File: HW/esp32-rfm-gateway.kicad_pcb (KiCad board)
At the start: 2 copper layers, 99 x 93.5 mm, 97 parts, among them J1 ph_1x2, J10 CS_1, J11 CS_1, J12 CS_1, J13 CS_1, J14 CS_1, J2 ph_1x2, J20 220V~, J21 ph_1x2, J22 s14500, J23 s18650, J24 ph_1x3, J25 ph_1x2, J3 ph_1x3, J30 AntSMA, J4 ph_1x4, J40 ph_1x2, J5 ph_1x4, J6 ph_1x3, J7 ph_1x4, J8 ph_1x4, Q20 IRLML2244, Q40 BC817, Q41 BC817, U1 ESP-WROOM-32, U10 PCA9633DP1, U2 BD48K30, U20 IRM-05, U21 MCP73832T-2ACI, U22 BD49K35, U23 TLV62569DBV, U24 TLV379IDBV, U30 RFM9x, U40 AT_CryptoAuth, U41 HIH8000_I2C

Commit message: Changes C4 to NC to prevent unwanted boot to Download mode and removes keepout area from under the ESP32 module.
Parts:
- C4: value 100nF -> 100nF-NC
- D20: value LED-DNP -> LED-NC
- R21: value 330-DNP -> 330-NC
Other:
- board text added: "rev.34"
- board text removed: "rev.33"
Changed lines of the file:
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@@
       (effects (font (size 1 1) (thickness 0.15)) (justify mirror))
     )
-    (fp_text value 330-DNP (at 0 2 90) (layer B.Fab)
+    (fp_text value 330-NC (at 0 2 90) (layer B.Fab)
       (effects (font (size 1 1) (thickness 0.15)) (justify mirror))
     )
@@
       (effects (font (size 1 1) (thickness 0.15)) (justify mirror))
     )
-    (fp_text value LED-DNP (at 0 1.5 270) (layer B.Fab)
+    (fp_text value LED-NC (at 0 1.5 270) (layer B.Fab)
       (effects (font (size 1 1) (thickness 0.15)) (justify mirror))
     )
@@
       (effects (font (size 1 1) (thickness 0.15)))
     )
-    (fp_text value 100nF (at 0 -2 270) (layer F.Fab)
+    (fp_text value 100nF-NC (at 0 -2 270) (layer F.Fab)
       (effects (font (size 1 1) (thickness 0.15)))
     )
@@
     (effects (font (size 1.5 1.5) (thickness 0.3)) (justify left mirror))
   )
-  (gr_text rev.33 (at 53 54) (layer F.SilkS)
+  (gr_text rev.34 (at 53 54) (layer F.SilkS)
     (effects (font (size 1.5 1.5) (thickness 0.3)))
   )
@@
       )
     )
-  )
-  (zone (net 0) (net_name "") (layers F&B.Cu) (hatch edge 0.508)
-    (connect_pads no (clearance 0.8))
-    (min_thickness 0.8)
-    (keepout (tracks allowed) (vias allowed) (copperpour not_allowed))
-    (fill (mode segment) (arc_segments 16) (thermal_gap 0.508) (thermal_bridge_width 0.508))
-    (polygon
-      (pts
-        (xy 93.5 51.75) (xy 97.5 51.75) (xy 97.5 65.75) (xy 93.5 65.75)
-      )
-    )

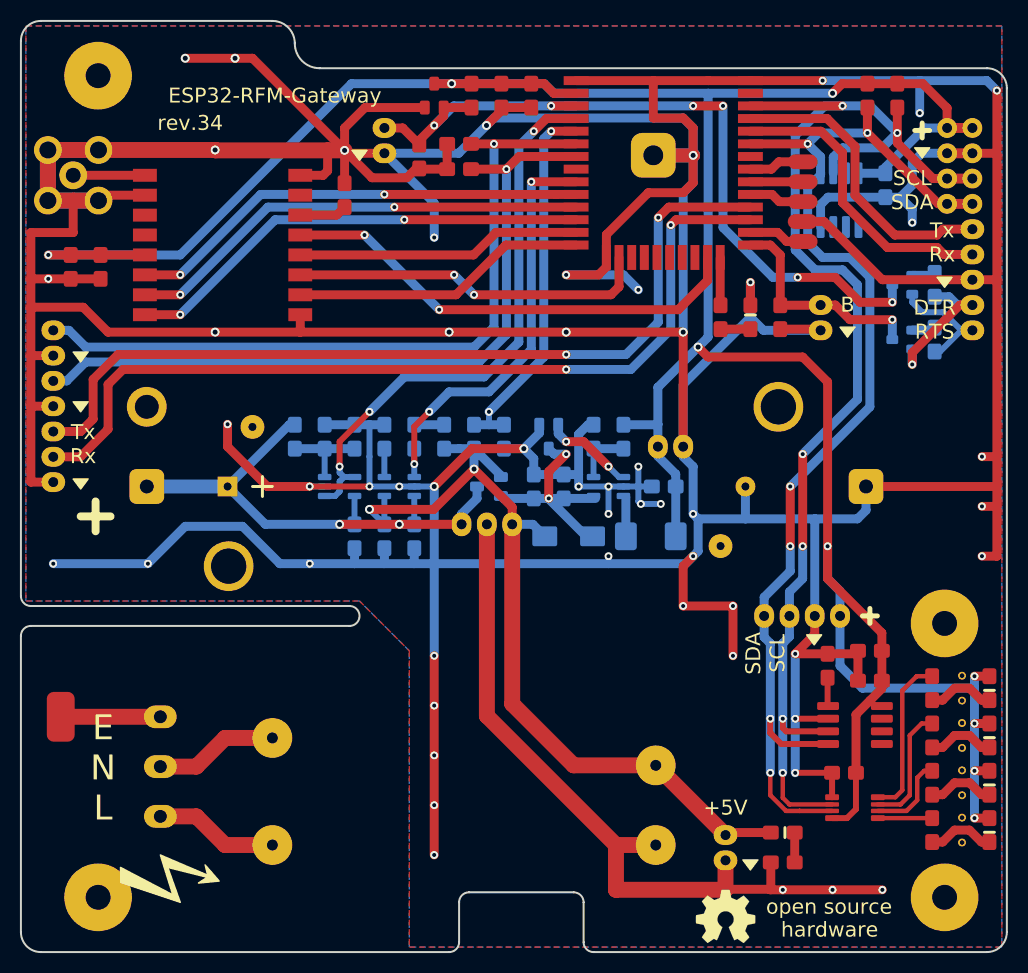
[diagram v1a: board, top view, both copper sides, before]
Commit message: Connects the LEDs straight to ESP32, removing the LED driver.
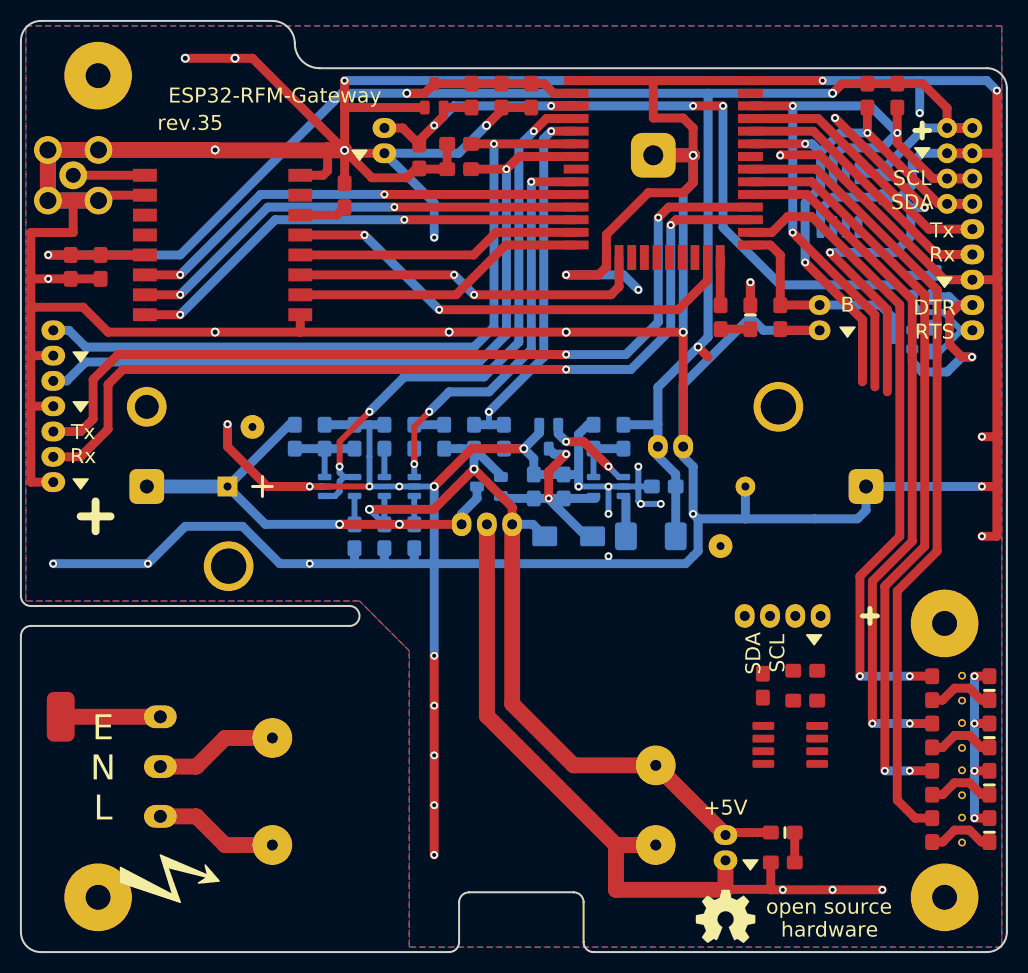
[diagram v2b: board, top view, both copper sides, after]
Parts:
- removed C10: 100nF, CalinGeneric:C0805HS
- removed C11: 4,7uF, CalinGeneric:C0805HS
- removed J10, J11, J12, J13, J14: CS_1, CalinConnectors:SMD_Pins_1x1
- removed U10: PCA9633DP1, CalinGeneric:TSSOP8-SOT505-1-HS
- added C43: 4,7uF, CalinGeneric:C0805HS, F.Cu at (114.8, 109.0)
- moved C41 6.80 mm to (110.5, 110.5)
- moved C42 6.80 mm to (114.8, 112.0)
- moved U41 6.80 mm to (113.2, 116.5)
- moved J8 1.95 mm to (116.3, 103.5)
- moved J2 0.10 mm to (116.2, 72.3)
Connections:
- R10 pad 2: Net-(R10-Pad2) -> /LED0
- R11 pad 2: Net-(R11-Pad2) -> /LED1
- R12 pad 2: Net-(R12-Pad2) -> /LED2
- R13 pad 2: Net-(R13-Pad2) -> /LED3
- U1 pad 26: /IO4 -> /LED3
- U1 pad 29: /IO5 -> /LED2
- U1 pad 30: /IO18 -> /LED1
- U1 pad 31: /IO19 -> /LED0
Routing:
- net +3V3: track 302.1 -> 214.0 mm, vias 9 -> 8
- net /LED0: track 0.00 -> 80.9 mm
- net /LED1: track 0.00 -> 76.4 mm, vias 0 -> 2
- net /LED2: track 0.00 -> 70.8 mm, vias 0 -> 2
- net /LED3: track 0.00 -> 65.5 mm, vias 0 -> 2
- net /SDA: track 118.1 -> 55.0 mm, vias 6 -> 3
- net /SCL: track 128.1 -> 69.1 mm, vias 6 -> 3
- net Net-(R13-Pad2): track 16.3 -> 0.00 mm
- net Net-(R12-Pad2): track 12.3 -> 0.00 mm
- net GND: track 926.0 -> 934.8 mm, vias 54 -> 51
- net Net-(R11-Pad2): track 8.44 -> 0.00 mm
- net /Additional Modules/DTR: track 14.9 -> 20.9 mm
- net /IO4: track 5.63 -> 0.00 mm
- net /IO19: track 5.55 -> 0.00 mm
- net /IO5: track 5.55 -> 0.00 mm
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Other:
- board text added: "rev.35"
- board text removed: "rev.34"

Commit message: Replaces the HIH8000 sensor with a HDC1080 sensor.
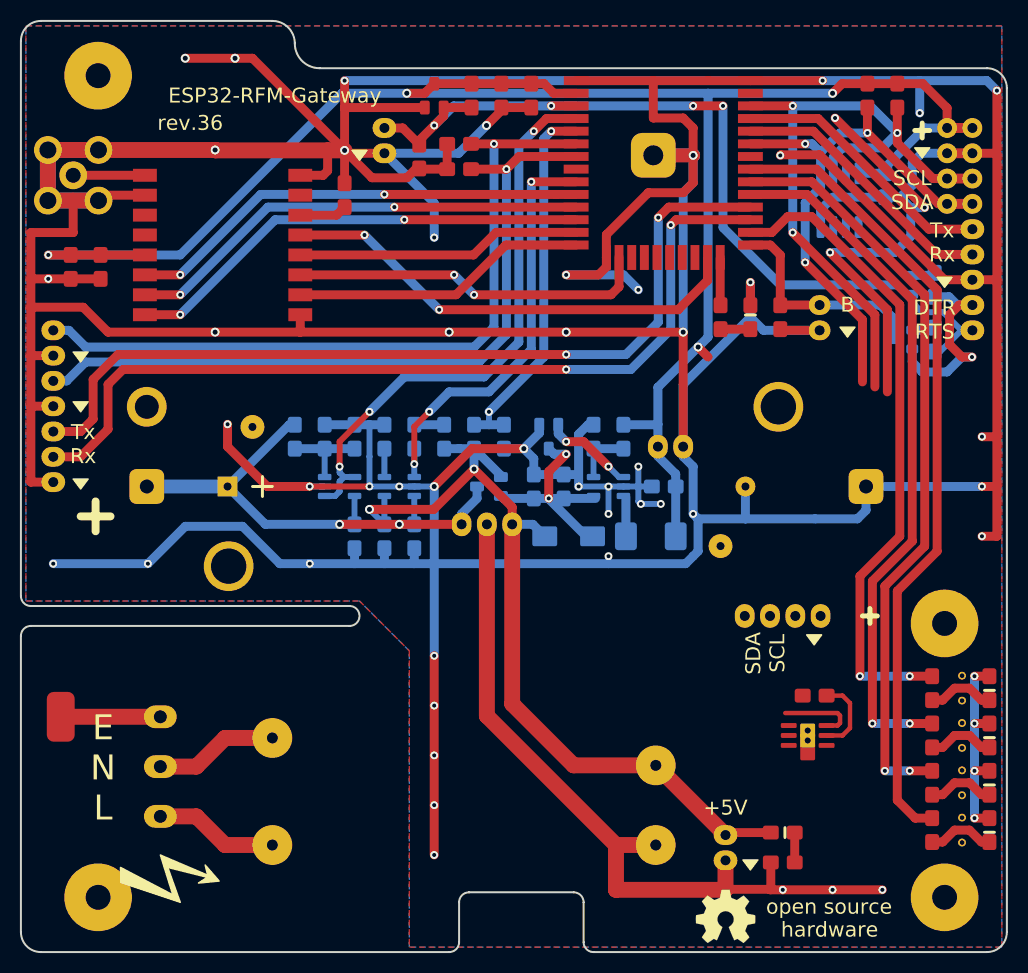
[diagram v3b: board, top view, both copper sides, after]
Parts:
- removed C42: 100nF, CalinGeneric:C0805HS
- removed C43: 4,7uF, CalinGeneric:C0805HS
- U41: value HIH8000_I2C -> HDC1080DMB; footprint CalinGeneric:SOIC-8-HS -> CalinGeneric:WSON6-TI-HDC-HS
- moved C41 5.30 mm to (115.7, 111.5), turned to 180 degrees
- moved U41 1.99 mm to (115.0, 115.5)
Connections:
- C41 pad 1: Net-(C41-Pad1) -> +3V3
- U41 pad 1: Net-(C41-Pad1) -> /SDA
- U41 pad 3: /SCL -> (no net)
- U41 pad 4: /SDA -> (no net)
- U41 pad 5: (no net) -> +3V3
- U41 pad 6: (no net) -> /SCL
- U41 pad 7: (no net) -> Net-(U41-Pad7)
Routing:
- net +3V3: track 214.0 -> 221.8 mm
- net /SCL: track 69.1 -> 76.9 mm
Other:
- board text added: "rev.36"
- board text removed: "rev.35"

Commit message: Extends the I2C connector J8 to have power pins on both side for extended compatibility with other modules.
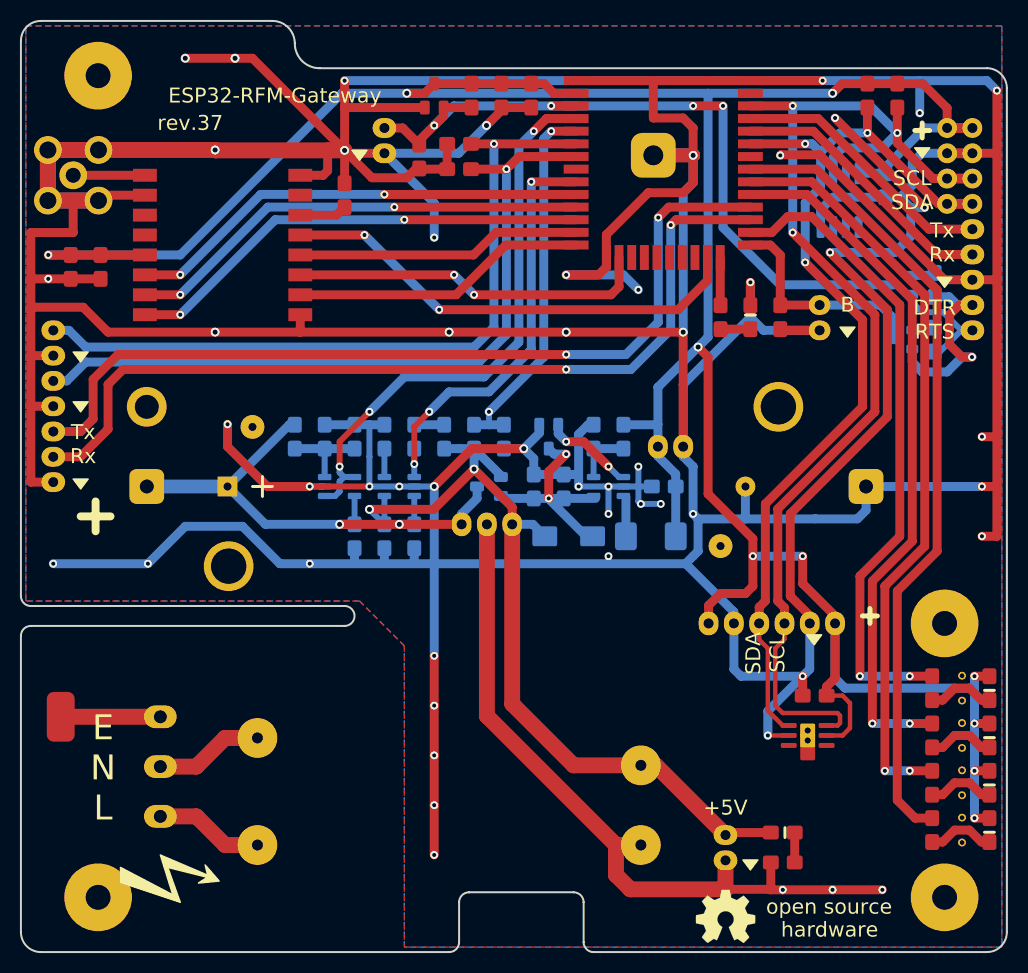
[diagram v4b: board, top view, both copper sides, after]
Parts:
- J8: value ph_1x4 -> ph_1x6; footprint CalinConnectors:Pin_Header_Straight_1x04 -> CalinConnectors:Pin_Header_Straight_1x06
- moved J8 1.63 mm to (117.8, 104.2)
- moved U20 1.50 mm to (79.0, 117.2)
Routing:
- net +3V3: track 221.8 -> 294.4 mm, vias 8 -> 10
- net GND: track 934.8 -> 997.4 mm, vias 51 -> 53
- net /SDA: track 55.0 -> 95.4 mm
- net /SCL: track 76.9 -> 115.0 mm
- net Net-(U41-Pad7): track 0.00 -> 2.15 mm
- net /Power Section/ACN: track 12.4 -> 10.9 mm
- net /Power Section/ACL: track 12.4 -> 10.9 mm
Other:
- outline, holes or cut-outs redrawn
- board text added: "rev.37"
- board text removed: "rev.36"

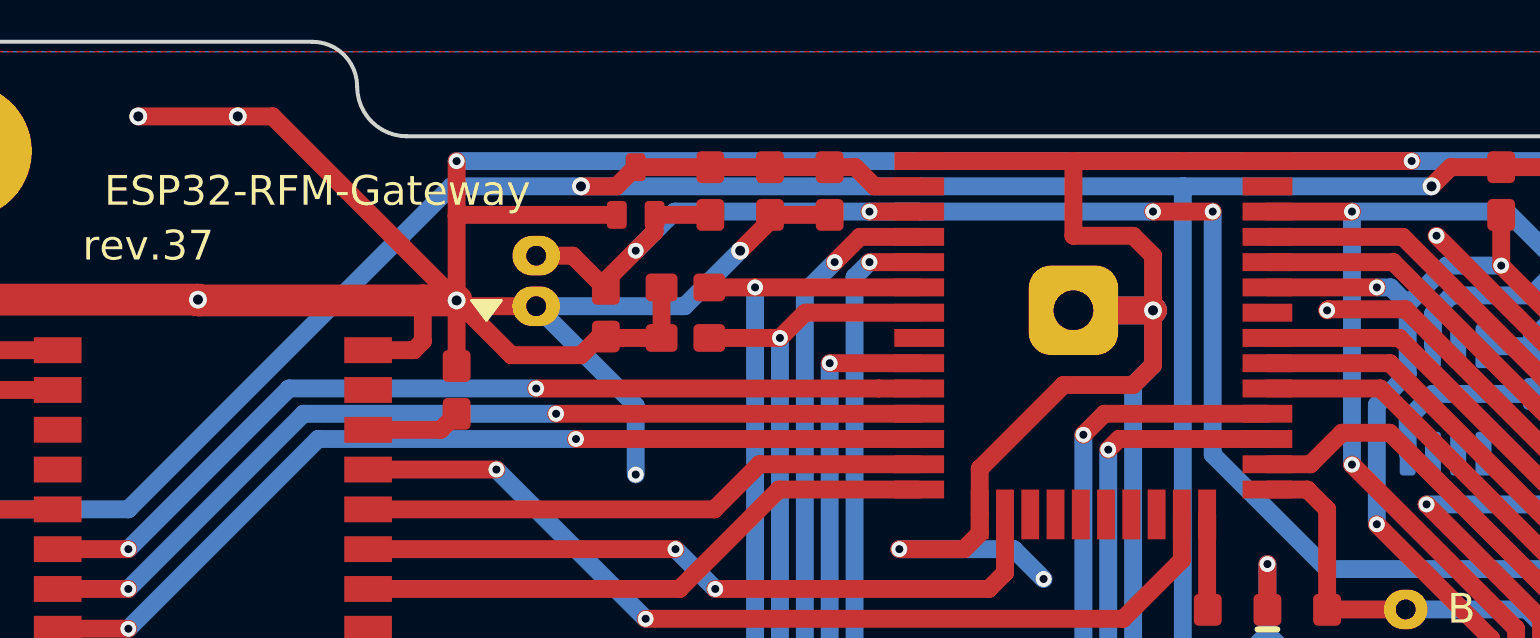
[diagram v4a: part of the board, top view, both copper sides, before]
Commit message: Improves component placement for ESP's power and reset circuitry
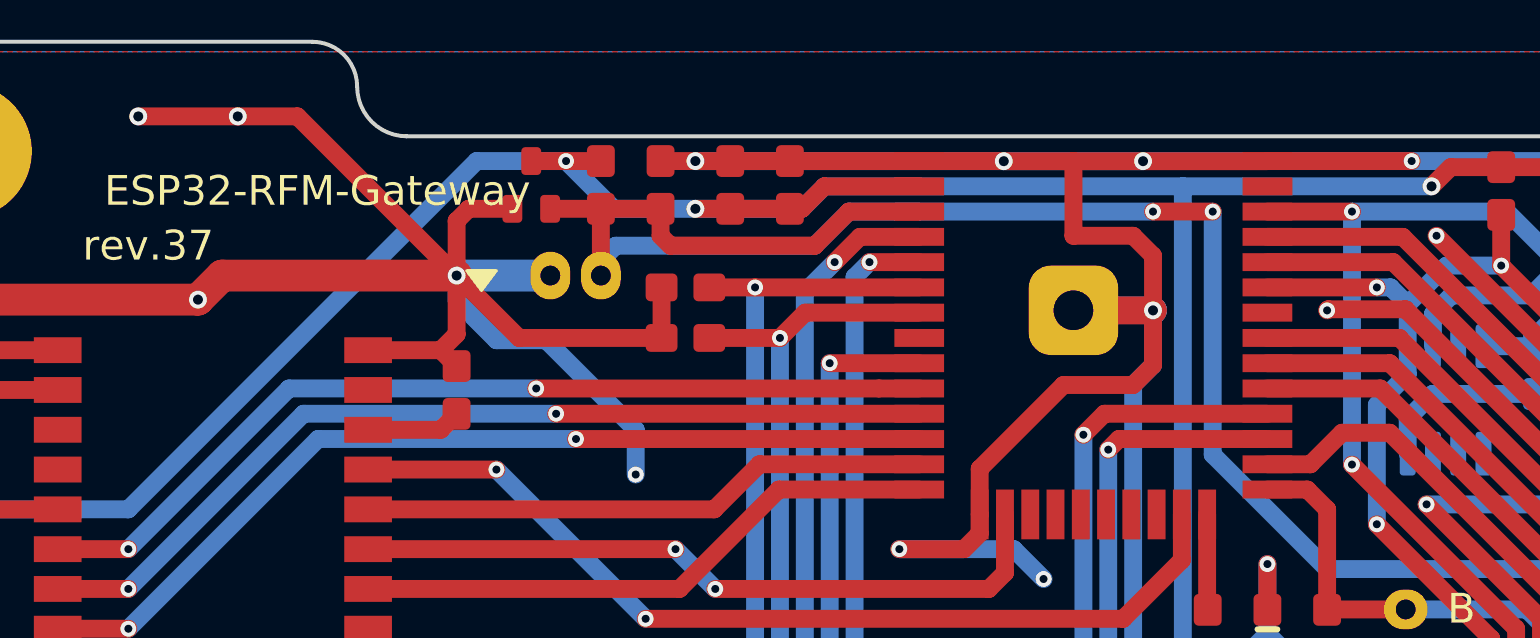
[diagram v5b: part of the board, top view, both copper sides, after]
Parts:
- moved C1 6.98 mm to (78.8, 50.9), turned to 90 degrees
- moved R1 5.51 mm to (75.8, 50.9)
- moved U2 5.26 mm to (72.2, 50.9)
- moved J1 3.40 mm to (75.8, 55.5), turned to 270 degrees
- moved C2 2.02 mm to (85.2, 50.9), turned to 90 degrees
- moved C3 2.02 mm to (82.2, 50.9), turned to 90 degrees
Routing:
- net GND: track 997.4 -> 977.8 mm, vias 53 -> 54
- net /Reset: track 75.6 -> 88.3 mm, vias 4 -> 2
- net +3V3: track 294.4 -> 293.8 mm, vias 10 -> 11
